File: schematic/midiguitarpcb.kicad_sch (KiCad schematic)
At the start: 37 parts, among them CN1 NMJ6HCD2, J1 USB_C_Receptacle_USB2.0_16P, SW1 SW_Omron_B3FS, U1 AMS1117-3.3, U2 DIN-504D-M5, U3 STM32H743ZITx

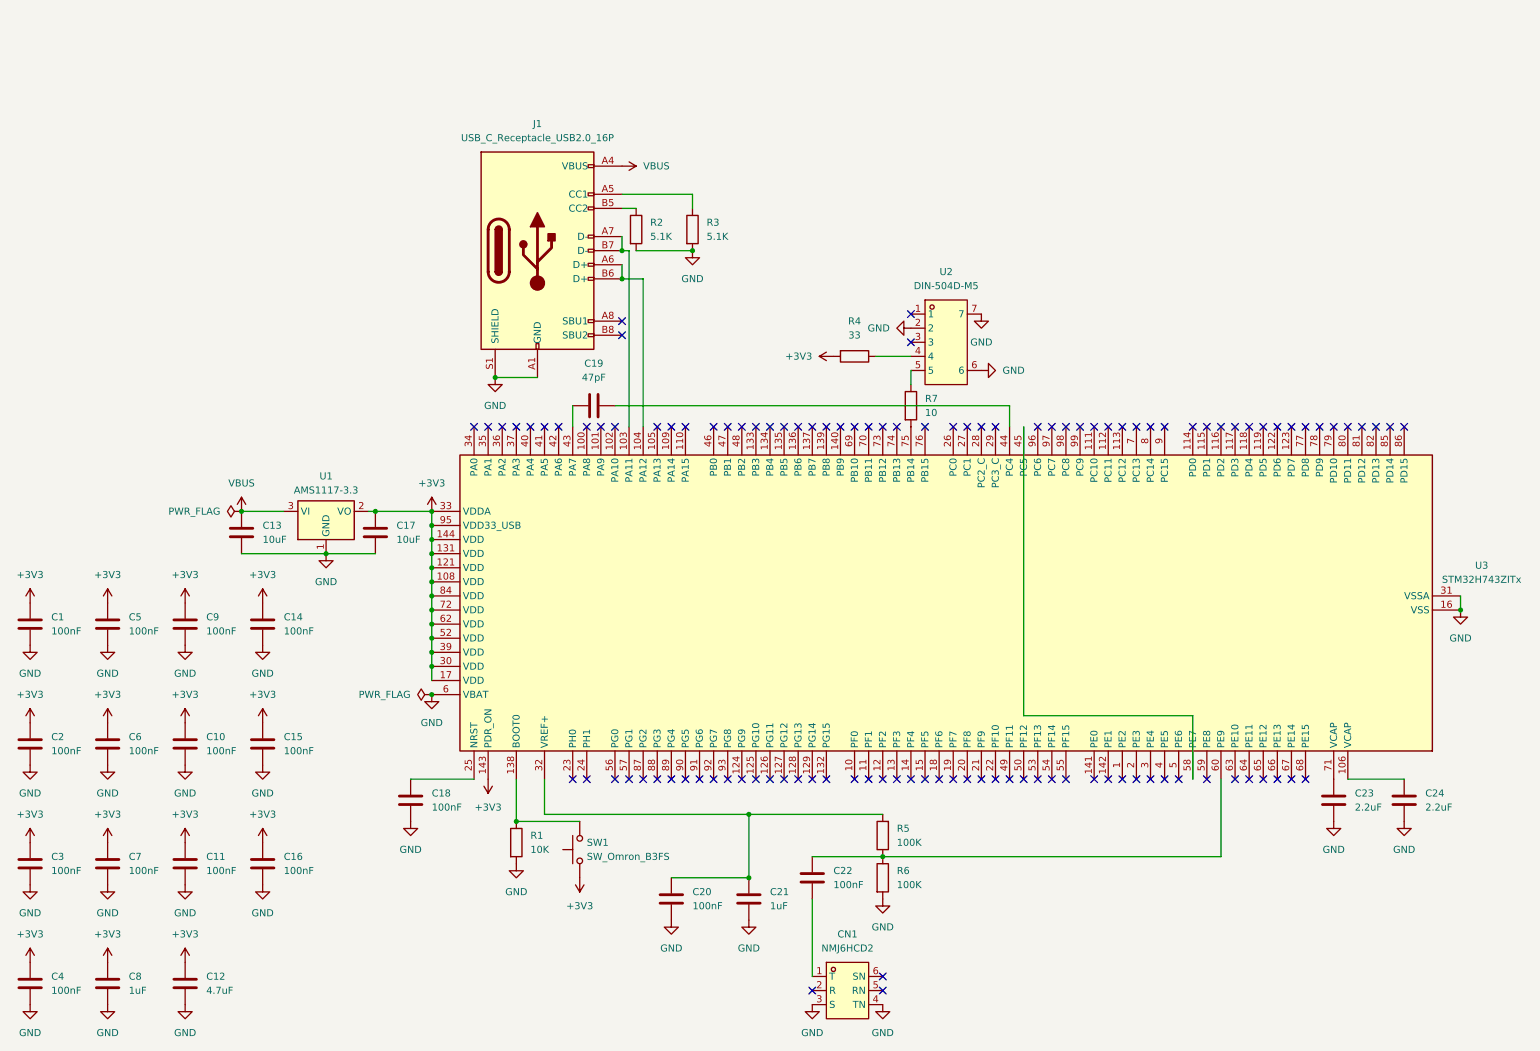
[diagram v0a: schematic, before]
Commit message: wip working but noisy
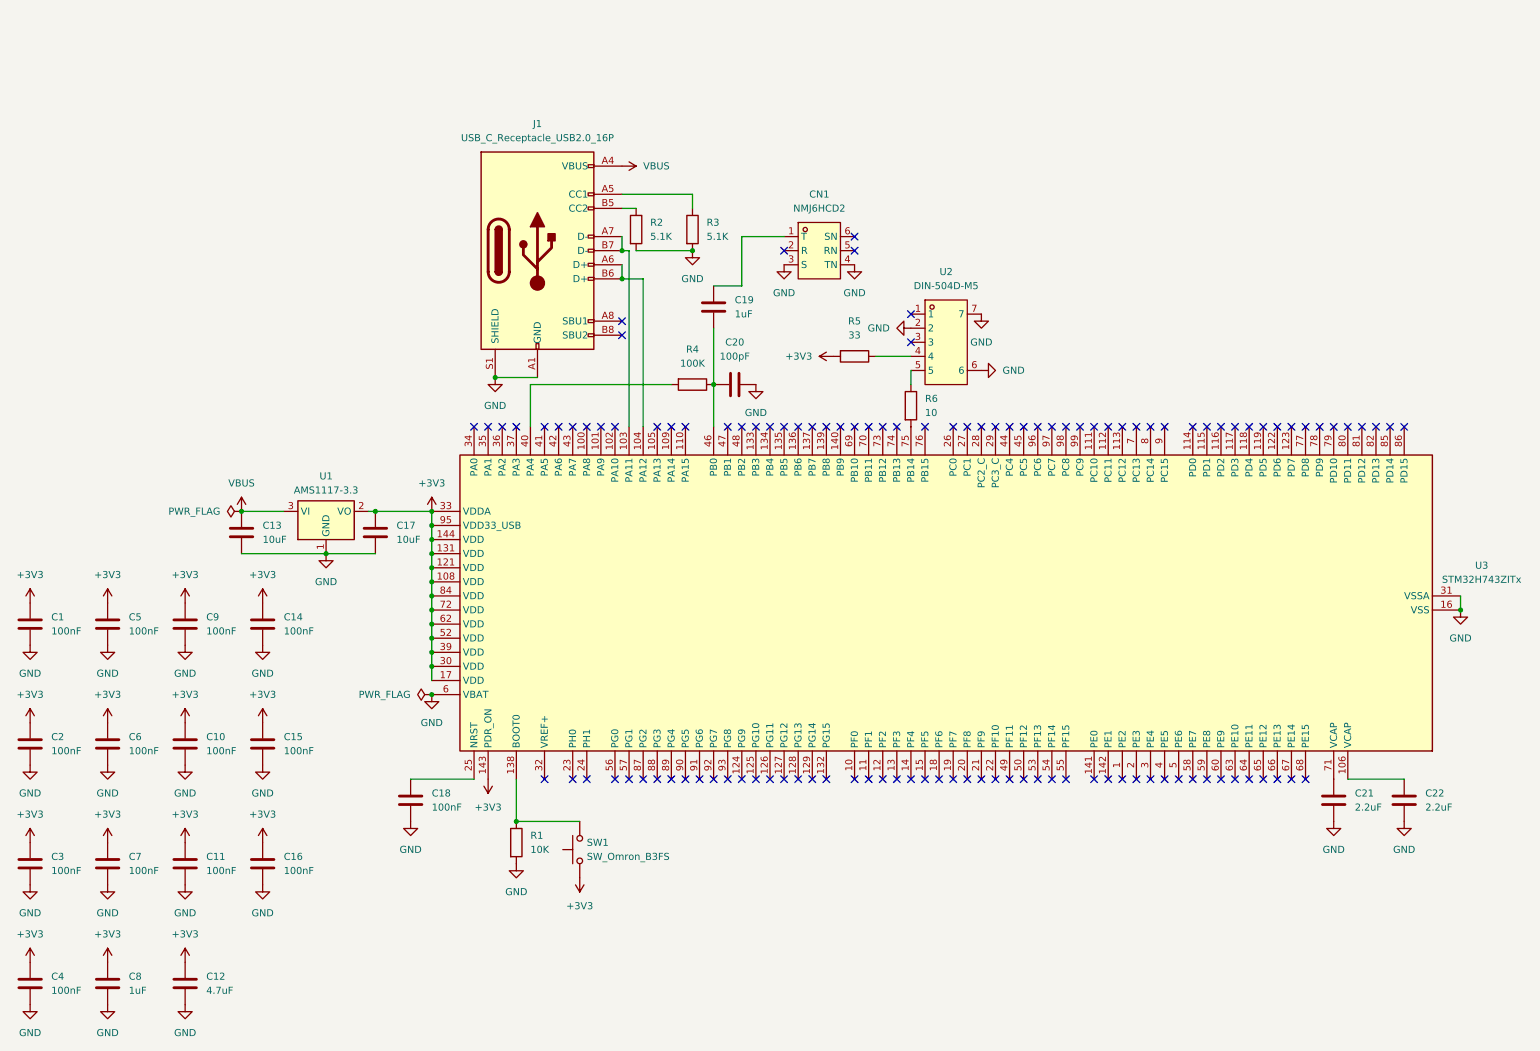
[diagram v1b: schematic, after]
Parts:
- removed C19: 47pF, Capacitor_SMD:C_0402_1005Metric, symbol Device:C
- removed C21: 1uF, Capacitor_SMD:C_0402_1005Metric, symbol Device:C
- removed R6: 100K, Resistor_SMD:R_0402_1005Metric, symbol Device:R
- C19: renamed from C22; value 100nF -> 1uF
- C20: value 100nF -> 100pF
- renumbered C23 to C21, C24 to C22, R5 to R4, R4 to R5, R7 to R6
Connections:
- net GND: now also C20.1; no longer C20.2
- net at U3.40 (PA4): now also R4.2
- net at U3.45 (PC5): no longer U3.58 (PE7)
- net at U3.46 (PB0): now also C19.1, C20.2, R4.1
- net at CN1.1 (T): now also C19.2; no longer C19.1
- now unconnected: U3.32 (VREF+), U3.60 (PE9)
- no-connect marks 113 -> 117
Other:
- moved on the sheet: C19, CN1, R4

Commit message: redo pcb
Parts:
- removed C1, C11, C14: 100nF, Capacitor_SMD:C_0402_1005Metric, symbol Device:C
- removed R4: 100K, Resistor_SMD:R_0402_1005Metric, symbol Device:R
- removed U3: STM32H743ZITx, Package_QFP:LQFP-144_20x20mm_P0.5mm, symbol MCU_ST_STM32H7:STM32H743ZITx
- added C21, C6, C7: 100nF, Capacitor_SMD:C_0805_2012Metric, symbol Device:C
- added FB1, FB2, FB3: 600@100MHz, Inductor_SMD:L_0805_2012Metric, symbol Device:FerriteBead
- added R6, R7, R8: 100K, Resistor_SMD:R_0805_2012Metric, symbol Device:R
- added R9: 0, Resistor_SMD:R_0805_2012Metric, symbol Device:R
- added U2: STM32H743VGTx, Package_QFP:LQFP-100_14x14mm_P0.5mm, symbol MCU_ST_STM32H7:STM32H743VGTx
- C1: renamed from C16; value 100nF -> 1uF; footprint Capacitor_SMD:C_0402_1005Metric -> Capacitor_SMD:C_0805_2012Metric
- C10: renamed from C17; footprint Capacitor_SMD:C_0402_1005Metric -> Capacitor_SMD:C_0805_2012Metric
- C11: renamed from C20; footprint Capacitor_SMD:C_0402_1005Metric -> Capacitor_SMD:C_0805_2012Metric
- C12: renamed from C2; footprint Capacitor_SMD:C_0402_1005Metric -> Capacitor_SMD:C_0805_2012Metric
- C13: renamed from C19; footprint Capacitor_SMD:C_0402_1005Metric -> Capacitor_SMD:C_0805_2012Metric
- C14: renamed from C21; footprint Capacitor_SMD:C_0402_1005Metric -> Capacitor_SMD:C_0805_2012Metric
- C15: renamed from C6; footprint Capacitor_SMD:C_0402_1005Metric -> Capacitor_SMD:C_0805_2012Metric
- C16: renamed from C22; footprint Capacitor_SMD:C_0402_1005Metric -> Capacitor_SMD:C_0805_2012Metric
- C17: renamed from C10; footprint Capacitor_SMD:C_0402_1005Metric -> Capacitor_SMD:C_0805_2012Metric
- C18: renamed from C15; footprint Capacitor_SMD:C_0402_1005Metric -> Capacitor_SMD:C_0805_2012Metric
- C19: renamed from C3; footprint Capacitor_SMD:C_0402_1005Metric -> Capacitor_SMD:C_0805_2012Metric
- C2: renamed from C8; value 1uF -> 100nF; footprint Capacitor_SMD:C_0402_1005Metric -> Capacitor_SMD:C_0805_2012Metric
- C20: renamed from C7; footprint Capacitor_SMD:C_0402_1005Metric -> Capacitor_SMD:C_0805_2012Metric
- C22: renamed from C12; footprint Capacitor_SMD:C_0402_1005Metric -> Capacitor_SMD:C_0805_2012Metric
- C3: renamed from C18; footprint Capacitor_SMD:C_0402_1005Metric -> Capacitor_SMD:C_0805_2012Metric
- C4, C9: value 100nF -> 1uF; footprint Capacitor_SMD:C_0402_1005Metric -> Capacitor_SMD:C_0805_2012Metric
- C5: footprint Capacitor_SMD:C_0402_1005Metric -> Capacitor_SMD:C_0805_2012Metric
- C8: renamed from C13; footprint Capacitor_SMD:C_0402_1005Metric -> Capacitor_SMD:C_0805_2012Metric
- R1: renamed from R5; footprint Resistor_SMD:R_0402_1005Metric -> Resistor_SMD:R_0805_2012Metric
- R2: renamed from R1; footprint Resistor_SMD:R_0402_1005Metric -> Resistor_SMD:R_0805_2012Metric
- R3: renamed from R6; footprint Resistor_SMD:R_0402_1005Metric -> Resistor_SMD:R_0805_2012Metric
- R4: renamed from R2; footprint Resistor_SMD:R_0402_1005Metric -> Resistor_SMD:R_0805_2012Metric
- R5: renamed from R3; footprint Resistor_SMD:R_0402_1005Metric -> Resistor_SMD:R_0805_2012Metric
- renumbered U2 to U1, U1 to U3
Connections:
- net +3V3: now also C21.1, FB1.1, U2.100 (VDD), U2.11 (VDD), U2.27 (VDD), U2.50 (VDD), U2.6 (VBAT), U2.75 (VDD); no longer C1.1, C2.1, C4.1, C5.1, C9.1
- net GND: now also C3.1, C21.2, C6.2, R9.1, U2.10 (VSS), U2.26 (VSS), U2.49 (VSS), U2.74 (VSS), U2.99 (VSS); no longer C1.2, C11.1, C2.2, C3.2, C4.2, C5.2, C9.2, CN1.3 (S), CN1.4 (TN)
- net at J1.A6 (D+), J1.B6 (D+): now also U2.70 (PA11)
- net at J1.A7 (D-), J1.B7 (D-): now also U2.69 (PA10)
- net at C11.2: now also U2.31 (PA7); no longer C13.1
- net at R1.1: now also FB2.1; no longer U1.4
- net at R3.1: now also FB3.1; no longer U1.5
- net at C14.1: now also U2.48 (VCAP)
- net at C16.1: now also U2.73 (VCAP)
- net at R2.1, SW1.2: now also U2.94 (BOOT0)
- net at R3.2: now also U2.68 (PA9)
- net at C13.2: now also R8.1, U2.33 (PC5); no longer CN1.1 (T)
- net VBUS: no longer names the net of C8.1, J1.A4 (VBUS), J1.A9 (VBUS), J1.B4 (VBUS), J1.B9 (VBUS), U3.3 (VI)
- net VBUS: now also C6.1
- new net: C1.1, C2.1, FB1.2, U2.21 (VDDA)
- new net: FB3.2, U1.5
- new net: C7.1, C9.1, R6.2, R7.1, R8.2, U2.34 (PB0)
- new net: C3.2, U2.14 (NRST)
- new net: C11.1, U2.32 (PC4)
- new net: FB2.2, U1.4
- new net: C13.1, CN1.1 (T)
- new net GNDA: C1.2, C2.2, C4.2, C5.2, C7.2, C9.2, CN1.3 (S), CN1.4 (TN), R7.2, R9.2, U2.19 (VSSA)
- new net VDDA: C4.1, C5.1, R6.1, U2.20 (VREF+)
- no-connect marks 117 -> 82
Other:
- moved on the sheet: C1, C10, C11, C12, C13, C14, C15, C16, C17, C18, C19, C2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

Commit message: wip about to put in mounting holes
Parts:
- added H1, H2, H3, H4: MountingHole_Pad_MP, MountingHole:MountingHole_3.2mm_M3_Pad, symbol Mechanical:MountingHole_Pad_MP
- added J1: Conn_ARM_SWD_TagConnect_TC2030, Connector:Tag-Connect_TC2030-IDC-FP_2x03_P1.27mm_Vertical, symbol Connector:Conn_ARM_SWD_TagConnect_TC2030
- renumbered C13 to C12, C12 to C13, J1 to J2
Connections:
- net +3V3: now also J1.1 (VCC)
- net GND: now also H1.MP, H2.MP, H3.MP, H4.MP, J1.5 (GND)
- net at J2.A6 (D+), J2.B6 (D+): now also U2.71 (PA12); no longer U2.70 (PA11)
- net at J2.A7 (D-), J2.B7 (D-): now also U2.70 (PA11); no longer U2.69 (PA10)
- net SWO: now reaches C12.2, R8.1, U2.33 (PC5)
- net SWO: now also J1.6 (SWO)
- net at C3.2, U2.14 (NRST): now also J1.3 (~{RESET})
- net SWDIO: now reaches U2.72 (PA13)
- net SWDIO: now also J1.2 (SWDIO)
- net SWCLK: now reaches U2.76 (PA14)
- net SWCLK: now also J1.4 (SWCLK)
- no-connect marks 82 -> 80
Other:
- moved on the sheet: C10, C13, C15, C17, C18, C19, C20, C21, C22, C6, C8, R4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

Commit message: wip about to put leds in
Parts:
- removed H1, H2, H3, H4: MountingHole_Pad_MP, MountingHole:MountingHole_3.2mm_M3_Pad, symbol Mechanical:MountingHole_Pad_MP
- added D1, D2: LED, LED_SMD:LED_0805_2012Metric, symbol Device:LED
- added H1, H2, H3, H4: MountingHole_Pad, MountingHole:MountingHole_3.2mm_M3_Pad, symbol Mechanical:MountingHole_Pad
- added R10, R9: 1K, Resistor_SMD:R_0805_2012Metric, symbol Device:R
- renumbered R9 to R11
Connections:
- net GND: now also D1.1 (K), D2.1 (K), H1.1, H2.1, H3.1, H4.1
- net SWO: now also U2.89 (PB3); no longer C12.2, R8.1, U2.33 (PC5)
- net at U2.65 (PC8): now also R9.1
- net at U2.66 (PC9): now also R10.1
- new net: D2.2 (A), R10.2
- new net: C12.2, R8.1, U2.33 (PC5)
- new net: D1.2 (A), R9.2
- no-connect marks 80 -> 77

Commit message: skinny pcb
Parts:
- C1, C10, C11, C12, C13, C14, C15, C16, C17, C18, C19, C2, C20, C21, C22, C3, C4, C5, C6, C7, C8, C9: footprint Capacitor_SMD:C_0805_2012Metric -> Capacitor_SMD:C_0603_1608Metric
- D1, D2: footprint LED_SMD:LED_0805_2012Metric -> LED_SMD:LED_0603_1608Metric
- FB1, FB2, FB3: footprint Inductor_SMD:L_0805_2012Metric -> Inductor_SMD:L_0603_1608Metric
- R1, R10, R11, R2, R3, R4, R5, R6, R7, R8, R9: footprint Resistor_SMD:R_0805_2012Metric -> Resistor_SMD:R_0603_1608Metric
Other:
- moved on the sheet: H2, H3, H4
